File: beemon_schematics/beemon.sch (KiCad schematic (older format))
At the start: 15 parts, among them SW1 SW_SPST, U1 TP4056mini, U2 AMS1117, U3 HD44780_I2C, U4 NodeMCU_1.0_(ESP-12E), U5 HX711

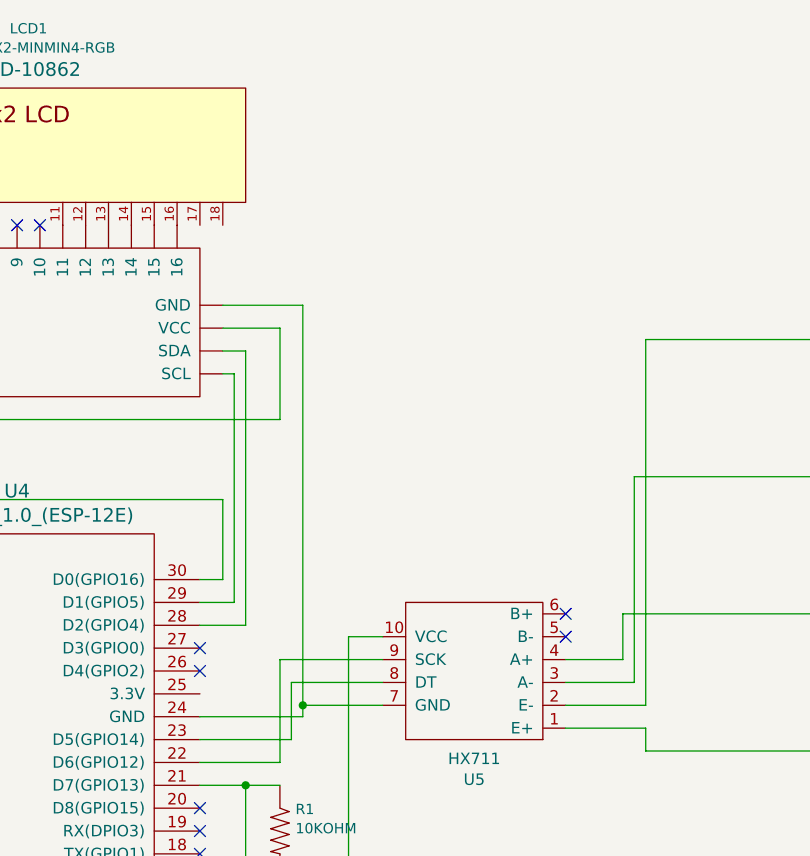
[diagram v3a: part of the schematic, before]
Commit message: Temp sensor added to compensate Seebeck effect. Weight sensors properly calibrated.
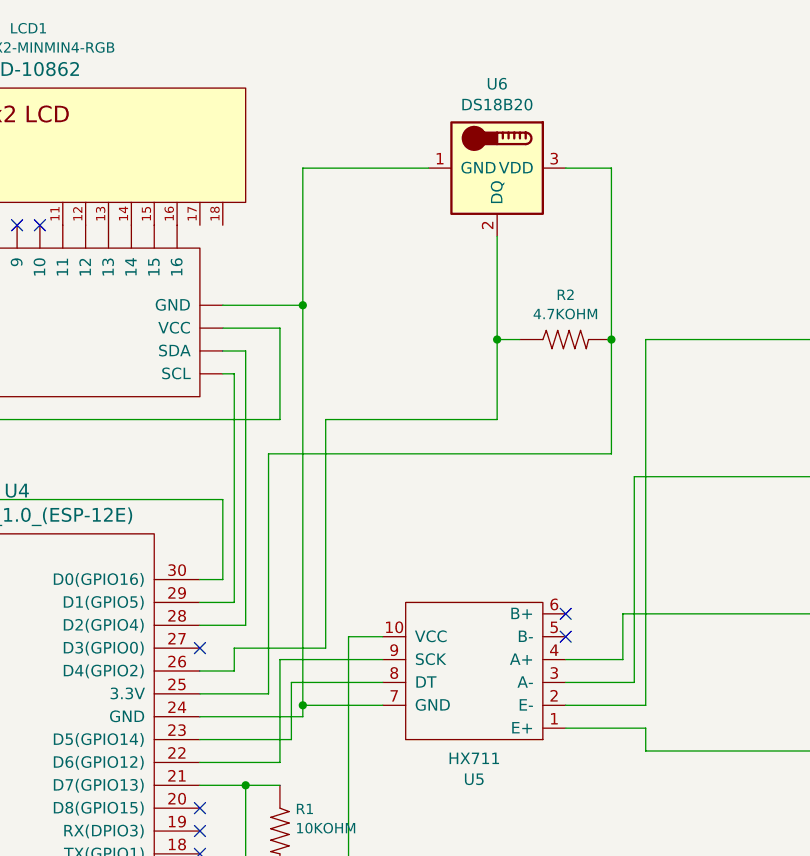
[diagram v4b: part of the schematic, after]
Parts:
- added R2: 4.7KOHM, 0603, symbol SparkFun-Resistors:4.7KOHM-0603-1_10W-1%
- added U6: DS18B20, Package_TO_SOT_THT:TO-92_Inline, symbol Sensor_Temperature:DS18B20
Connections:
- net at U3.~ (VCC), U4.24 (GND), U5.7 (GND): now also U6.1 (GND)
- net at U4.25 (3.3V): now also R2.2, U6.3 (VDD)
- net at U4.26 (D4(GPIO2)): now also R2.1, U6.2 (DQ)
- no-connect marks 22 -> 21
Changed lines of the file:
@@
 NoConn ~ 5000 4650
 NoConn ~ 6600 3850
-NoConn ~ 6600 3950
 NoConn ~ 6600 4550
 NoConn ~ 6600 4650
@@
 NoConn ~ 8200 3700
 NoConn ~ 8200 3800
+$Comp
+L Sensor_Temperature:DS18B20 U6
+U 1 1 6089228E
+P 7900 1750
+F 0 "U6" V 7533 1750 50  0000 C CNN
+F 1 "DS18B20" V 7624 1750 50  0000 C CNN
+F 2 "Package_TO_SOT_THT:TO-92_Inline" H 6900 1500 50  0001 C CNN
+F 3 "http://datasheets.maximintegrated.com/en/ds/DS18B20.pdf" H 7750 2000 50  0001 C CNN
+	1    7900 1750
+	0    1    1    0
+$EndComp
+Wire Wire Line
+	7600 1750 7050 1750
+Wire Wire Line
+	7050 1750 7050 2350
+Connection ~ 7050 2350
+Wire Wire Line
+	6600 4050 6900 4050
+Wire Wire Line
+	6900 4050 6900 3000
+Wire Wire Line
+	6600 3950 6750 3950
+Wire Wire Line
+	6750 3950 6750 3850
+Wire Wire Line
+	6750 3850 7150 3850
+Wire Wire Line
+	7150 3850 7150 2850
+Wire Wire Line
+	7150 2850 7900 2850
+Wire Wire Line
+	7900 2850 7900 2500
+Wire Wire Line
+	8400 3000 8400 2500
+Wire Wire Line
+	8400 1750 8200 1750
+Wire Wire Line
+	6900 3000 8400 3000
+$Comp
+L SparkFun-Resistors:4.7KOHM-0603-1_10W-1% R2
+U 1 1 608A5C7F
+P 8200 2500
+F 0 "R2" H 8200 2694 45  0000 C CNN
+F 1 "4.7KOHM" H 8200 2610 45  0000 C CNN
+F 2 "0603" H 8200 2650 20  0001 C CNN
+F 3 "" H 8200 2500 60  0001 C CNN
+F 4 "" H 8200 2621 60  0000 C CNN "Field4"
+	1    8200 2500
+	1    0    0    -1
+$EndComp
+Connection ~ 8400 2500
+Wire Wire Line
+	8400 2500 8400 1750
+Wire Wire Line
+	8000 2500 7900 2500
+Connection ~ 7900 2500
+Wire Wire Line
+	7900 2500 7900 2050
 $EndSCHEMATC

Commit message: Value checks
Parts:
- added BT2: Battery_Cell, symbol Device:Battery_Cell
- added R3: 220KOHM, 0603, symbol SparkFun-Resistors:220KOHM-0603-1_10W-1%
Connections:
- net at BT1.1 (+), U1.3 (BAT+), U2.3 (VI)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: now also BT2.1 (+)
- net at U4.11 (3.3V): now also R3.2
- net at BT1.2 (-), SW1.2 (B), U1.4 (BAT-)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: now also BT2.2 (-)
- net at U4.8 (SDO(MISO)): now also R3.1
- no-connect marks 21 -> 19
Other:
- moved on the sheet: SW1
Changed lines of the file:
@@
 Title "BeeMon"
 Date "2021-04-13"
-Rev "1.1"
+Rev "2.0"
 Comp ""
 Comment1 ""
@@
 $EndComp
 Wire Wire Line
-	3850 3550 3150 3550
+	3850 3550 3450 3550
 Wire Wire Line
 	3150 3550 3150 3600
@@
 	3350 3800 3350 3850
 Wire Wire Line
-	3350 3850 3850 3850
+	3350 3850 3450 3850
 Wire Wire Line
 	3850 4850 5000 4850
@@
 NoConn ~ 5000 4050
 NoConn ~ 5000 4150
-NoConn ~ 5000 4250
 NoConn ~ 5000 4350
 NoConn ~ 5000 4450
-NoConn ~ 5000 4550
 NoConn ~ 5000 4650
 NoConn ~ 6600 3850
@@
 L Switch:SW_SPST SW1
 U 1 1 607C3174
-P 4450 4300
-F 0 "SW1" V 4496 4212 50  0000 R CNN
-F 1 "SW_SPST" V 4405 4212 50  0000 R CNN
-F 2 "" H 4450 4300 50  0001 C CNN
-F 3 "~" H 4450 4300 50  0001 C CNN
-	1    4450 4300
+P 4000 4300
+F 0 "SW1" V 4046 4212 50  0000 R CNN
+F 1 "SW_SPST" V 3955 4212 50  0000 R CNN
+F 2 "" H 4000 4300 50  0001 C CNN
+F 3 "~" H 4000 4300 50  0001 C CNN
+	1    4000 4300
 	0    -1   -1   0
 $EndComp
@@
 	3850 3850 3850 4850
 Wire Wire Line
-	4850 4750 4450 4750
-Wire Wire Line
-	4450 4750 4450 4500
-Connection ~ 4850 4750
-Wire Wire Line
-	4450 4100 4450 3850
-Wire Wire Line
-	4450 3850 3850 3850
-Wire Wire Line
 	8550 4300 9550 4300
 NoConn ~ 8200 3700
@@
 Wire Wire Line
 	7900 2500 7900 2050
+$Comp
+L SparkFun-Resistors:220KOHM-0603-1_10W-1% R3
+U 1 1 608C7991
+P 4500 4350
+F 0 "R3" V 4458 4418 45  0000 L CNN
+F 1 "220KOHM" V 4542 4418 45  0000 L CNN
+F 2 "0603" H 4500 4500 20  0001 C CNN
+F 3 "" H 4500 4350 60  0001 C CNN
+F 4 "" V 4584 4418 60  0000 L CNN "Field4"
+	1    4500 4350
+	0    1    1    0
+$EndComp
+Wire Wire Line
+	4850 4750 4000 4750
+Wire Wire Line
+	4000 4750 4000 4500
+Connection ~ 4850 4750
+Wire Wire Line
+	3850 3850 4000 3850
+Wire Wire Line
+	4000 3850 4000 4100
+Wire Wire Line
+	5000 4550 4500 4550
+Wire Wire Line
+	5000 4250 4800 4250
+Wire Wire Line
+	4800 4250 4800 4150
+Wire Wire Line
+	4800 4150 4500 4150
+$Comp
+L Device:Battery_Cell BT2
+U 1 1 608BE395
+P 3450 3750
+F 0 "BT2" V 3195 3800 50  0000 C CNN
+F 1 "Battery_Cell" V 3286 3800 50  0000 C CNN
+F 2 "" V 3450 3810 50  0001 C CNN
+F 3 "~" V 3450 3810 50  0001 C CNN
+	1    3450 3750
+	1    0    0    -1
+$EndComp
+Connection ~ 3450 3550
+Wire Wire Line
+	3450 3550 3150 3550
+Connection ~ 3450 3850
+Wire Wire Line
+	3450 3850 3850 3850
 $EndSCHEMATC
